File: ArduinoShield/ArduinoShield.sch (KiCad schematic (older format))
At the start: 2 parts, among them J1 Conn_02x20_Odd_Even

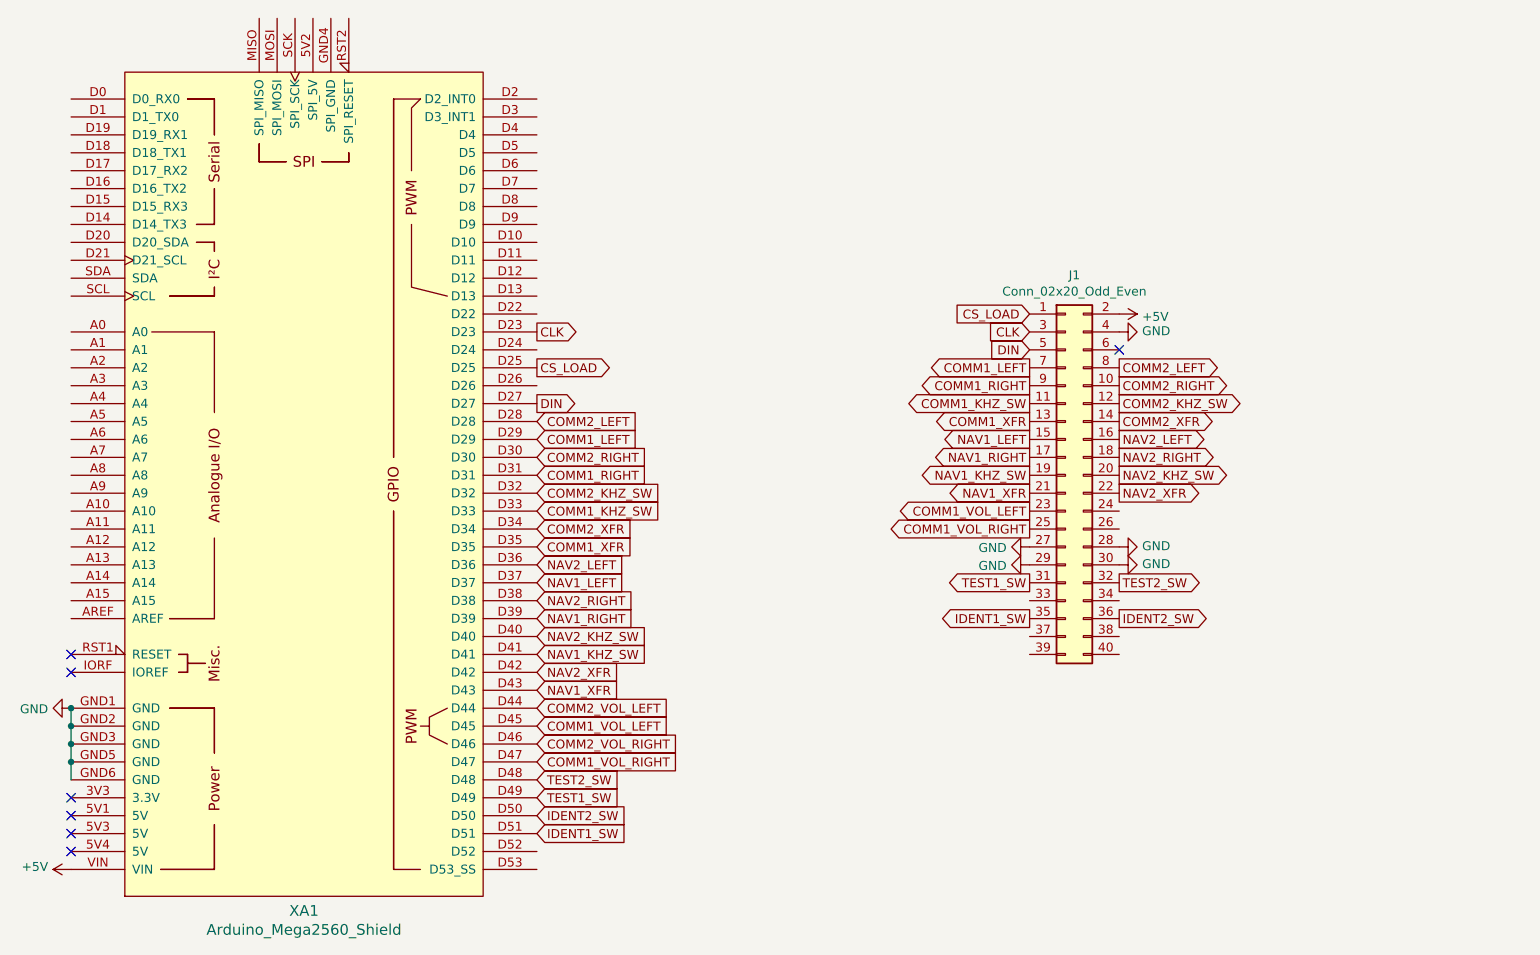
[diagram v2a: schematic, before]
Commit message: Arduino shield plus more main board changes
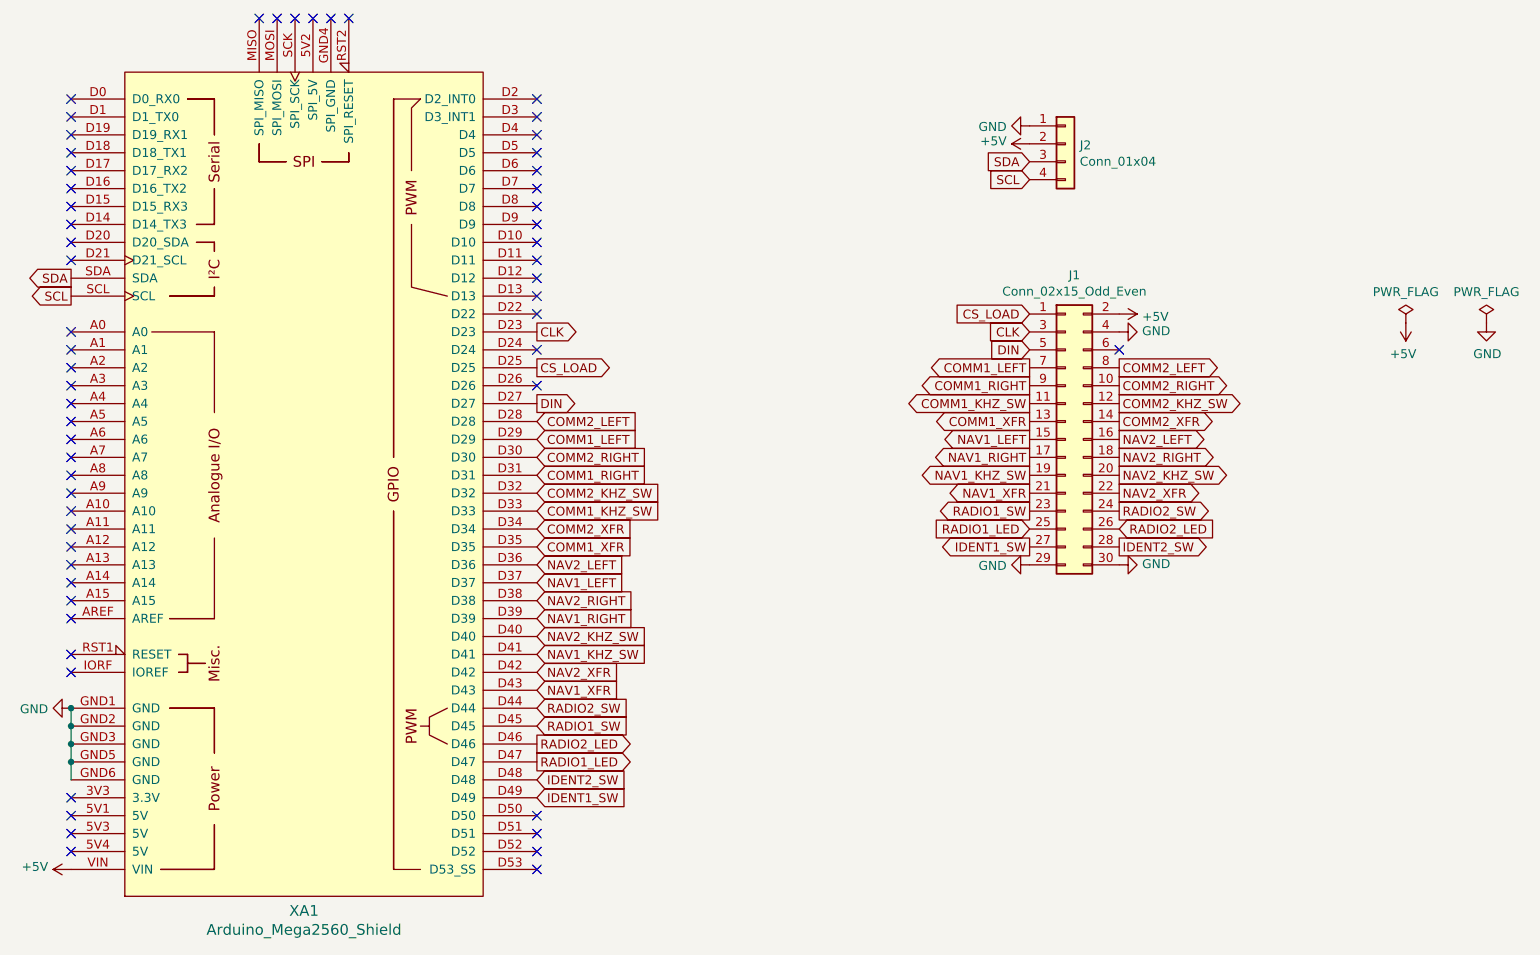
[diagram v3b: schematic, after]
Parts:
- removed J1: Conn_02x20_Odd_Even, symbol Connector_Generic:Conn_02x20_Odd_Even
- added J1: Conn_02x15_Odd_Even, Connector_PinSocket_2.54mm:PinSocket_2x15_P2.54mm_Vertical, symbol Connector_Generic:Conn_02x15_Odd_Even
- added J2: Conn_01x04, Arduino Shield:Molex_KK-254_AE-6410-04A_1x04_P2.54mm_Horizontal, symbol Connector_Generic:Conn_01x04
- XA1: footprint (none) -> Arduino:Arduino_Mega2560_Shield
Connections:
- net TEST1_SW is gone; now on net IDENT1_SW: XA1.D49
- net TEST2_SW is gone; now on net IDENT2_SW: XA1.D48
- net +5V: now also J1.2 (Pin_2), J2.2 (Pin_2)
- net CLK: now also J1.3 (Pin_3)
- net COMM1_KHZ_SW: now also J1.11 (Pin_11)
- net COMM1_LEFT: now also J1.7 (Pin_7)
- net COMM1_RIGHT: now also J1.9 (Pin_9)
- net COMM1_XFR: now also J1.13 (Pin_13)
- net COMM2_KHZ_SW: now also J1.12 (Pin_12)
- net COMM2_LEFT: now also J1.8 (Pin_8)
- net COMM2_RIGHT: now also J1.10 (Pin_10)
- net COMM2_XFR: now also J1.14 (Pin_14)
- net CS_LOAD: now also J1.1 (Pin_1)
- net DIN: now also J1.5 (Pin_5)
- net GND: now also J1.29 (Pin_29), J1.30 (Pin_30), J1.4 (Pin_4), J2.1 (Pin_1)
- net IDENT1_SW: now also J1.27 (Pin_27); no longer XA1.D51
- net IDENT2_SW: now also J1.28 (Pin_28); no longer XA1.D50
- net NAV1_KHZ_SW: now also J1.19 (Pin_19)
- net NAV1_LEFT: now also J1.15 (Pin_15)
- net NAV1_RIGHT: now also J1.17 (Pin_17)
- net NAV1_XFR: now also J1.21 (Pin_21)
- net NAV2_KHZ_SW: now also J1.20 (Pin_20)
- net NAV2_LEFT: now also J1.16 (Pin_16)
- net NAV2_RIGHT: now also J1.18 (Pin_18)
- net NAV2_XFR: now also J1.22 (Pin_22)
- net SCL: now reaches XA1.SCL
- net SCL: now also J2.4 (Pin_4)
- net SDA: now reaches XA1.SDA
- net SDA: now also J2.3 (Pin_3)
- net COMM1_VOL_LEFT renamed RADIO1_SW
- net RADIO1_SW: now also J1.23 (Pin_23)
- net COMM1_VOL_RIGHT renamed RADIO1_LED
- net RADIO1_LED: now also J1.25 (Pin_25)
- net COMM2_VOL_LEFT renamed RADIO2_SW
- net RADIO2_SW: now also J1.24 (Pin_24)
- net COMM2_VOL_RIGHT renamed RADIO2_LED
- net RADIO2_LED: now also J1.26 (Pin_26)
- no-connect marks 7 -> 59
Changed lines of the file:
@@
 F 0 "XA1" H 3400 1319 60  0000 C CNN
 F 1 "Arduino_Mega2560_Shield" H 3400 1213 60  0000 C CNN
-F 2 "" H 4100 6450 60  0001 C CNN
+F 2 "Arduino:Arduino_Mega2560_Shield" H 4100 6450 60  0001 C CNN
 F 3 "" H 4100 6450 60  0001 C CNN
 	1    3400 3700
-	1    0    0    -1
-$EndComp
-$Comp
-L Connector_Generic:Conn_02x20_Odd_Even J1
-U 1 1 5F6987E2
-P 7650 3650
-F 0 "J1" H 7700 4767 50  0000 C CNN
-F 1 "Conn_02x20_Odd_Even" H 7700 4676 50  0000 C CNN
-F 2 "" H 7650 3650 50  0001 C CNN
-F 3 "~" H 7650 3650 50  0001 C CNN
-	1    7650 3650
 	1    0    0    -1
 $EndComp
@@
 L power:GND #PWR05
 U 1 1 5F69A9AD
+P 7450 4150
+F 0 "#PWR05" H 7450 3900 50  0001 C CNN
+F 1 "GND" V 7455 4022 50  0000 R CNN
+F 2 "" H 7450 4150 50  0001 C CNN
+F 3 "" H 7450 4150 50  0001 C CNN
+	1    7450 4150
+	0    1    1    0
+$EndComp
+$Comp
+L power:GND #PWR04
+U 1 1 5F69ACF5
 P 7950 4150
-F 0 "#PWR05" H 7950 3900 50  0001 C CNN
+F 0 "#PWR04" H 7950 3900 50  0001 C CNN
 F 1 "GND" V 7955 4022 50  0000 R CNN
 F 2 "" H 7950 4150 50  0001 C CNN
 F 3 "" H 7950 4150 50  0001 C CNN
 	1    7950 4150
-	0    -1   -1   0
-$EndComp
-$Comp
-L power:GND #PWR04
-U 1 1 5F69ACF5
-P 7950 4050
-F 0 "#PWR04" H 7950 3800 50  0001 C CNN
-F 1 "GND" V 7955 3922 50  0000 R CNN
-F 2 "" H 7950 4050 50  0001 C CNN
-F 3 "" H 7950 4050 50  0001 C CNN
-	1    7950 4050
 	0    -1   -1   0
 $EndComp
@@
 Text GLabel 4700 4650 2    50   Input ~ 0
 NAV1_KHZ_SW
+Text GLabel 7450 3850 0    50   Output ~ 0
+RADIO1_SW
 Text GLabel 4700 5050 2    50   Input ~ 0
-COMM1_VOL_LEFT
-Text GLabel 4700 5250 2    50   Input ~ 0
-COMM1_VOL_RIGHT
-Text GLabel 7450 3850 0    50   Output ~ 0
-COMM1_VOL_LEFT
-Text GLabel 7450 3950 0    50   Output ~ 0
-COMM1_VOL_RIGHT
-$Comp
-L power:GND #PWR?
-U 1 1 5F6A5DCE
-P 7450 4050
-F 0 "#PWR?" H 7450 3800 50  0001 C CNN
-F 1 "GND" V 7455 3922 50  0000 R CNN
-F 2 "" H 7450 4050 50  0001 C CNN
-F 3 "" H 7450 4050 50  0001 C CNN
-	1    7450 4050
-	0    1    1    0
-$EndComp
-$Comp
-L power:GND #PWR?
-U 1 1 5F6A618F
-P 7450 4150
-F 0 "#PWR?" H 7450 3900 50  0001 C CNN
-F 1 "GND" V 7455 4022 50  0000 R CNN
-F 2 "" H 7450 4150 50  0001 C CNN
-F 3 "" H 7450 4150 50  0001 C CNN
-	1    7450 4150
-	0    1    1    0
-$EndComp
-Text GLabel 7450 4250 0    50   Output ~ 0
-TEST1_SW
-Text GLabel 4700 5450 2    50   Input ~ 0
-TEST1_SW
+RADIO1_SW
 Text GLabel 7950 3050 2    50   Output ~ 0
 COMM2_LEFT
@@
 COMM2_KHZ_SW
 $Comp
-L power:GND #PWR?
+L power:GND #PWR08
 U 1 1 5F6A881F
 P 7950 2850
-F 0 "#PWR?" H 7950 2600 50  0001 C CNN
+F 0 "#PWR08" H 7950 2600 50  0001 C CNN
 F 1 "GND" V 7955 2722 50  0000 R CNN
 F 2 "" H 7950 2850 50  0001 C CNN
@@
 Text GLabel 4700 4850 2    50   Input ~ 0
 NAV1_XFR
+Text GLabel 4700 4950 2    50   Input ~ 0
+RADIO2_SW
+Text GLabel 7950 3850 2    50   Output ~ 0
+RADIO2_SW
+Text GLabel 7950 4050 2    50   Output ~ 0
+IDENT2_SW
+Text GLabel 4700 5450 2    50   Input ~ 0
+IDENT1_SW
 Text GLabel 4700 5350 2    50   Input ~ 0
-TEST2_SW
-Text GLabel 7950 4250 2    50   Output ~ 0
-TEST2_SW
-Text GLabel 7950 4450 2    50   Output ~ 0
 IDENT2_SW
-Text GLabel 4700 5650 2    50   Input ~ 0
+Text GLabel 7450 4050 0    50   Output ~ 0
 IDENT1_SW
-Text GLabel 4700 5550 2    50   Input ~ 0
-IDENT2_SW
-Text GLabel 7450 4450 0    50   Output ~ 0
-IDENT1_SW
-Text GLabel 4700 4950 2    50   Input ~ 0
-COMM2_VOL_LEFT
-Text GLabel 4700 5150 2    50   Input ~ 0
-COMM2_VOL_RIGHT
+Text GLabel 7450 3950 0    50   Input ~ 0
+RADIO1_LED
+Text GLabel 7950 3950 2    50   Input ~ 0
+RADIO2_LED
+Text GLabel 4700 5150 2    50   Output ~ 0
+RADIO2_LED
+Text GLabel 4700 5250 2    50   Output ~ 0
+RADIO1_LED
+$Comp
+L Connector_Generic:Conn_01x04 J2
+U 1 1 5F6C280E
+P 7650 1800
+F 0 "J2" H 7730 1792 50  0000 L CNN
+F 1 "Conn_01x04" H 7730 1701 50  0000 L CNN
+F 2 "Arduino Shield:Molex_KK-254_AE-6410-04A_1x04_P2.54mm_Horizontal" H 7650 1800 50  0001 C CNN
+F 3 "~" H 7650 1800 50  0001 C CNN
+	1    7650 1800
+	1    0    0    -1
+$EndComp
+$Comp
+L power:GND #PWR06
+U 1 1 5F6C33B2
+P 7450 1700
+F 0 "#PWR06" H 7450 1450 50  0001 C CNN
+F 1 "GND" V 7455 1572 50  0000 R CNN
+F 2 "" H 7450 1700 50  0001 C CNN
+F 3 "" H 7450 1700 50  0001 C CNN
+	1    7450 1700
+	0    1    1    0
+$EndComp
+$Comp
+L power:+5V #PWR07
+U 1 1 5F6C370B
+P 7450 1800
+F 0 "#PWR07" H 7450 1650 50  0001 C CNN
+F 1 "+5V" V 7465 1928 50  0000 L CNN
+F 2 "" H 7450 1800 50  0001 C CNN
+F 3 "" H 7450 1800 50  0001 C CNN
+	1    7450 1800
+	0    -1   -1   0
+$EndComp
+Text GLabel 7450 1900 0    50   Input ~ 0
+SDA
+Text GLabel 7450 2000 0    50   Input ~ 0
+SCL
+Text GLabel 2100 2550 0    50   Output ~ 0
+SDA
+Text GLabel 2100 2650 0    50   Output ~ 0
+SCL
+NoConn ~ 2100 1550
+NoConn ~ 2100 1650
+NoConn ~ 2100 1750
+NoConn ~ 2100 1850
+NoConn ~ 2100 1950
+NoConn ~ 2100 2050
+NoConn ~ 2100 2150
+NoConn ~ 2100 2250
+NoConn ~ 2100 2350
+NoConn ~ 2100 2450
+NoConn ~ 2100 2850
+NoConn ~ 2100 2950
+NoConn ~ 2100 3050
+NoConn ~ 2100 3150
+NoConn ~ 2100 3250
+NoConn ~ 2100 3350
+NoConn ~ 2100 3450
+NoConn ~ 2100 3550
+NoConn ~ 2100 3650
+NoConn ~ 2100 3750
+NoConn ~ 2100 3850
+NoConn ~ 2100 3950
+NoConn ~ 2100 4050
+NoConn ~ 2100 4150
+NoConn ~ 2100 4250
+NoConn ~ 2100 4350
+NoConn ~ 2100 4450
+NoConn ~ 3150 1100
+NoConn ~ 3250 1100
+NoConn ~ 3350 1100
+NoConn ~ 3450 1100
+NoConn ~ 3550 1100
+NoConn ~ 3650 1100
+NoConn ~ 4700 1550
+NoConn ~ 4700 1650
+NoConn ~ 4700 1750
+NoConn ~ 4700 1850
+NoConn ~ 4700 1950
+NoConn ~ 4700 2050
+NoConn ~ 4700 2150
+NoConn ~ 4700 2250
+NoConn ~ 4700 2350
+NoConn ~ 4700 2450
+NoConn ~ 4700 2550
+NoConn ~ 4700 2650
+NoConn ~ 4700 2750
+NoConn ~ 4700 2950
+NoConn ~ 4700 3150
+$Comp
+L Connector_Generic:Conn_02x15_Odd_Even J1
+U 1 1 5F6C8193
+P 7650 3450
+F 0 "J1" H 7700 4367 50  0000 C CNN
+F 1 "Conn_02x15_Odd_Even" H 7700 4276 50  0000 C CNN
+F 2 "Connector_PinSocket_2.54mm:PinSocket_2x15_P2.54mm_Vertical" H 7650 3450 50  0001 C CNN
+F 3 "~" H 7650 3450 50  0001 C CNN
+	1    7650 3450
+	1    0    0    -1
+$EndComp
+NoConn ~ 4700 5550
+NoConn ~ 4700 5650
+NoConn ~ 4700 5750
+NoConn ~ 4700 5850
+$Comp
+L power:PWR_FLAG #FLG0101
+U 1 1 5F6CB2FC
+P 9550 2800
+F 0 "#FLG0101" H 9550 2875 50  0001 C CNN
+F 1 "PWR_FLAG" H 9550 2973 50  0000 C CNN
+F 2 "" H 9550 2800 50  0001 C CNN
+F 3 "~" H 9550 2800 50  0001 C CNN
+	1    9550 2800
+	1    0    0    -1
+$EndComp
+$Comp
+L power:PWR_FLAG #FLG0102
+U 1 1 5F6CBB1C
+P 10000 2800
+F 0 "#FLG0102" H 10000 2875 50  0001 C CNN
+F 1 "PWR_FLAG" H 10000 2973 50  0000 C CNN
+F 2 "" H 10000 2800 50  0001 C CNN
+F 3 "~" H 10000 2800 50  0001 C CNN
+	1    10000 2800
+	1    0    0    -1
+$EndComp
+$Comp
+L power:+5V #PWR0101
+U 1 1 5F6CBE49
+P 9550 2800
+F 0 "#PWR0101" H 9550 2650 50  0001 C CNN
+F 1 "+5V" H 9565 2973 50  0000 C CNN
+F 2 "" H 9550 2800 50  0001 C CNN
+F 3 "" H 9550 2800 50  0001 C CNN
+	1    9550 2800
+	-1   0    0    1
+$EndComp
+$Comp
+L power:GND #PWR0102
+U 1 1 5F6CC190
+P 10000 2800
+F 0 "#PWR0102" H 10000 2550 50  0001 C CNN
+F 1 "GND" H 10005 2627 50  0000 C CNN
+F 2 "" H 10000 2800 50  0001 C CNN
+F 3 "" H 10000 2800 50  0001 C CNN
+	1    10000 2800
+	1    0    0    -1
+$EndComp
 $EndSCHEMATC

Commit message: Finally done maybe for real
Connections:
- net CLK: now also XA1.D49; no longer XA1.D23
- net COMM1_KHZ_SW: now also XA1.D41; no longer XA1.D33
- net COMM1_LEFT: now also XA1.D45; no longer XA1.D29
- net COMM1_RIGHT: now also XA1.D43; no longer XA1.D31
- net COMM1_XFR: now also XA1.D39; no longer XA1.D35
- net COMM2_KHZ_SW: now also XA1.D40; no longer XA1.D32
- net COMM2_LEFT: now also XA1.D44; no longer XA1.D28
- net COMM2_RIGHT: now also XA1.D42; no longer XA1.D30
- net COMM2_XFR: now also XA1.D38; no longer XA1.D34
- net CS_LOAD: now also XA1.D51; no longer XA1.D25
- net DIN: now also XA1.D47; no longer XA1.D27
- net IDENT1_SW: now also XA1.D25; no longer XA1.D49
- net IDENT2_SW: now also XA1.D24; no longer XA1.D48
- net NAV1_KHZ_SW: now also XA1.D33; no longer XA1.D41
- net NAV1_RIGHT: now also XA1.D35; no longer XA1.D39
- net NAV1_XFR: now also XA1.D31; no longer XA1.D43
- net NAV2_KHZ_SW: now also XA1.D32; no longer XA1.D40
- net NAV2_RIGHT: now also XA1.D34; no longer XA1.D38
- net NAV2_XFR: now also XA1.D30; no longer XA1.D42
- net RADIO1_LED: now also XA1.D27; no longer XA1.D47
- net RADIO1_SW: now also XA1.D29; no longer XA1.D45
- net RADIO2_LED: now also XA1.D26; no longer XA1.D46
- net RADIO2_SW: now also XA1.D28; no longer XA1.D44
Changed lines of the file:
@@
 NoConn ~ 2100 4650
 NoConn ~ 2100 4750
-Text GLabel 4700 3250 2    50   Output ~ 0
+Text GLabel 4700 5250 2    50   Output ~ 0
 DIN
-Text GLabel 4700 3050 2    50   Output ~ 0
+Text GLabel 4700 5650 2    50   Output ~ 0
 CS_LOAD
-Text GLabel 4700 2850 2    50   Output ~ 0
+Text GLabel 4700 5450 2    50   Output ~ 0
 CLK
 Text GLabel 7450 2950 0    50   Input ~ 0
@@
 Text GLabel 7450 3250 0    50   Output ~ 0
 COMM1_KHZ_SW
-Text GLabel 4700 3850 2    50   Input ~ 0
+Text GLabel 4700 4650 2    50   Input ~ 0
 COMM1_KHZ_SW
 Text GLabel 7450 3050 0    50   Output ~ 0
@@
 Text GLabel 7450 3150 0    50   Output ~ 0
 COMM1_RIGHT
-Text GLabel 4700 3450 2    50   Input ~ 0
+Text GLabel 4700 5050 2    50   Input ~ 0
 COMM1_LEFT
-Text GLabel 4700 3650 2    50   Input ~ 0
+Text GLabel 4700 4850 2    50   Input ~ 0
 COMM1_RIGHT
 Text GLabel 7450 3450 0    50   Output ~ 0
@@
 Text GLabel 4700 4250 2    50   Input ~ 0
 NAV1_LEFT
-Text GLabel 4700 4450 2    50   Input ~ 0
+Text GLabel 4700 4050 2    50   Input ~ 0
 NAV1_RIGHT
-Text GLabel 4700 4650 2    50   Input ~ 0
+Text GLabel 4700 3850 2    50   Input ~ 0
 NAV1_KHZ_SW
 Text GLabel 7450 3850 0    50   Output ~ 0
 RADIO1_SW
-Text GLabel 4700 5050 2    50   Input ~ 0
+Text GLabel 4700 3450 2    50   Input ~ 0
 RADIO1_SW
 Text GLabel 7950 3050 2    50   Output ~ 0
@@
 Text GLabel 7950 3250 2    50   Output ~ 0
 COMM2_KHZ_SW
-Text GLabel 4700 3350 2    50   Input ~ 0
+Text GLabel 4700 4950 2    50   Input ~ 0
 COMM2_LEFT
-Text GLabel 4700 3550 2    50   Input ~ 0
+Text GLabel 4700 4750 2    50   Input ~ 0
 COMM2_RIGHT
-Text GLabel 4700 3750 2    50   Input ~ 0
+Text GLabel 4700 4550 2    50   Input ~ 0
 COMM2_KHZ_SW
 $Comp
@@
 Text GLabel 4700 4150 2    50   Input ~ 0
 NAV2_LEFT
+Text GLabel 4700 3950 2    50   Input ~ 0
+NAV2_RIGHT
+Text GLabel 4700 3750 2    50   Input ~ 0
+NAV2_KHZ_SW
 Text GLabel 4700 4350 2    50   Input ~ 0
-NAV2_RIGHT
-Text GLabel 4700 4550 2    50   Input ~ 0
-NAV2_KHZ_SW
-Text GLabel 4700 3950 2    50   Input ~ 0
 COMM2_XFR
-Text GLabel 4700 4050 2    50   Input ~ 0
+Text GLabel 4700 4450 2    50   Input ~ 0
 COMM1_XFR
 Text GLabel 7950 3450 2    50   Output ~ 0
@@
 Text GLabel 7950 3750 2    50   Output ~ 0
 NAV2_XFR
-Text GLabel 4700 4750 2    50   Input ~ 0
+Text GLabel 4700 3550 2    50   Input ~ 0
 NAV2_XFR
-Text GLabel 4700 4850 2    50   Input ~ 0
+Text GLabel 4700 3650 2    50   Input ~ 0
 NAV1_XFR
-Text GLabel 4700 4950 2    50   Input ~ 0
+Text GLabel 4700 3350 2    50   Input ~ 0
 RADIO2_SW
 Text GLabel 7950 3850 2    50   Output ~ 0
@@
 Text GLabel 7950 4050 2    50   Output ~ 0
 IDENT2_SW
-Text GLabel 4700 5450 2    50   Input ~ 0
+Text GLabel 4700 3050 2    50   Input ~ 0
 IDENT1_SW
-Text GLabel 4700 5350 2    50   Input ~ 0
+Text GLabel 4700 2950 2    50   Input ~ 0
 IDENT2_SW
 Text GLabel 7450 4050 0    50   Output ~ 0
@@
 Text GLabel 7950 3950 2    50   Input ~ 0
 RADIO2_LED
-Text GLabel 4700 5150 2    50   Output ~ 0
+Text GLabel 4700 3150 2    50   Output ~ 0
 RADIO2_LED
-Text GLabel 4700 5250 2    50   Output ~ 0
+Text GLabel 4700 3250 2    50   Output ~ 0
 RADIO1_LED
 $Comp
@@
 NoConn ~ 4700 2650
 NoConn ~ 4700 2750
-NoConn ~ 4700 2950
-NoConn ~ 4700 3150
 $Comp
 L Connector_Generic:Conn_02x15_Odd_Even J1
@@
 	1    0    0    -1
 $EndComp
-NoConn ~ 4700 5550
-NoConn ~ 4700 5650
 NoConn ~ 4700 5750
 NoConn ~ 4700 5850
@@
 	1    0    0    -1
 $EndComp
+NoConn ~ 4700 5150
+NoConn ~ 4700 5350
+NoConn ~ 4700 2850
+NoConn ~ 4700 5550
 $EndSCHEMATC
